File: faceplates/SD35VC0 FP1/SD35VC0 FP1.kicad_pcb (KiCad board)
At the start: 2 copper layers, 101.5 x 25.8 mm, 15 parts, among them M1 Mounting_Pin, M10 Mounting_Pad, M2 Mounting_Pin, M3 Mounting_Pin, M4 Mounting_Pin, M5 Mounting_Pad, M6 Mounting_Pad, M7 Mounting_Pad, M8 Mounting_Pad, M9 Mounting_Pad

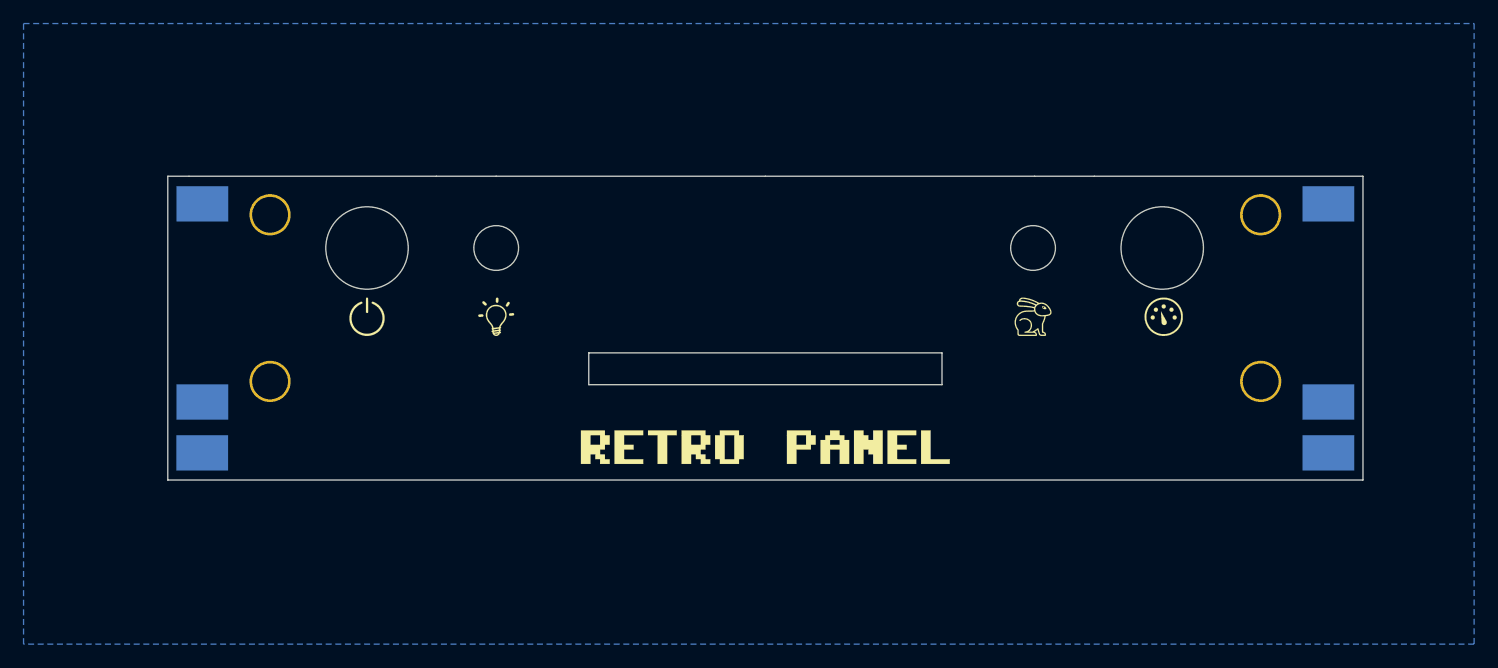
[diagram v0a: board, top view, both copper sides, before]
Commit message: Adjust faceplate cutouts
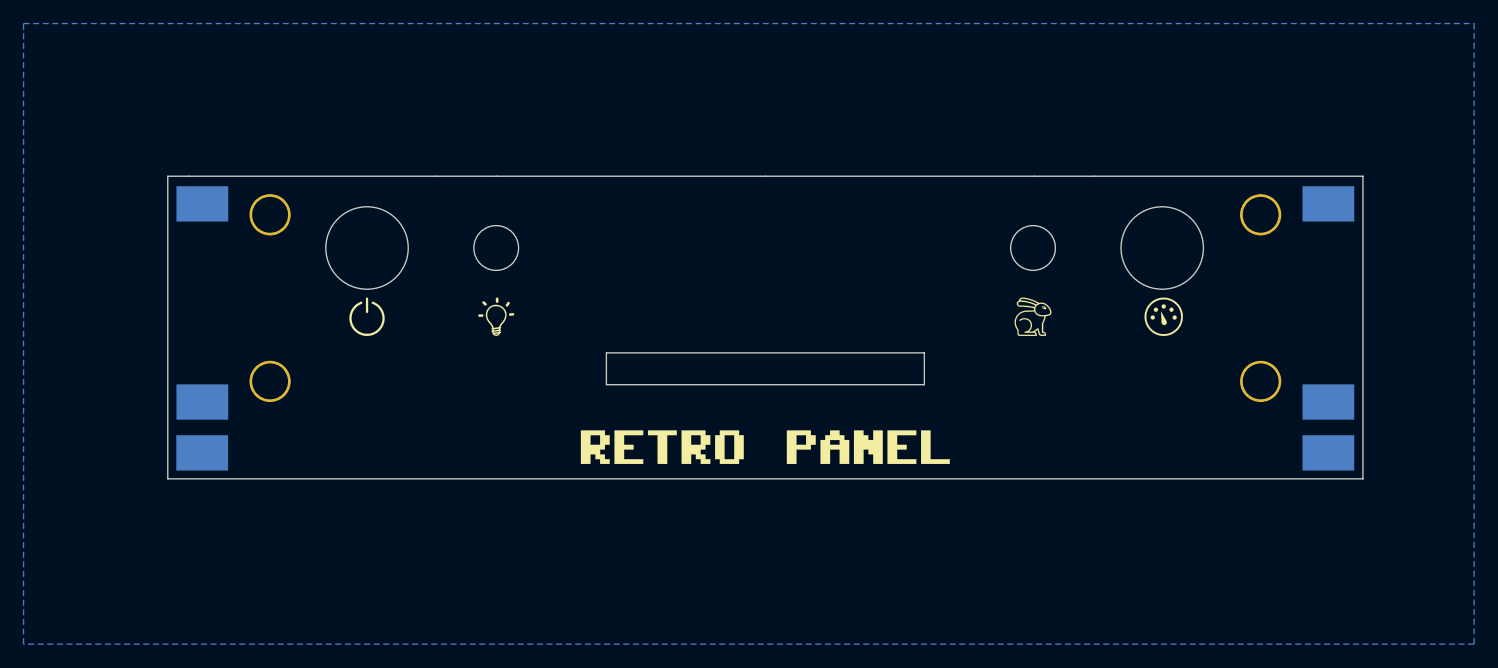
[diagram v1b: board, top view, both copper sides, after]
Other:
- board size 101.5 x 25.8 mm -> 101.5 x 25.7 mm
- board text added: "3.5" RetroPanel SD35VC0 FP1 Faceplate FP1 (rev. B) github.com/tebl"
- board text removed: "3.5" RetroPanel SD35VC0 FP1 Faceplate FP1 (rev. A) github.com/tebl"
